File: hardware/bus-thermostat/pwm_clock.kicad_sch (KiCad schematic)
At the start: 16 parts, among them U12 NE555PWR, U14 TLV9301IDCK, U16 TLV9301IDCK

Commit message: Update some components
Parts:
- added TP1: TestPoint, Connector_Pin:Pin_D0.7mm_L6.5mm_W1.8mm_FlatFork, symbol Connector:TestPoint
- TP2: renamed from TP?; footprint (none) -> Connector_Pin:Pin_D0.7mm_L6.5mm_W1.8mm_FlatFork
- gave numbers to parts that had none: 2
- renumbered C27 to C26, C28 to C27, C30 to C28, C31 to C29, C32 to C30, R44 to R41, U12 to U11, U14 to U12, U16 to U13
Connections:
- net at C29.1, U12.3 (-), U12.4: now also TP1.1

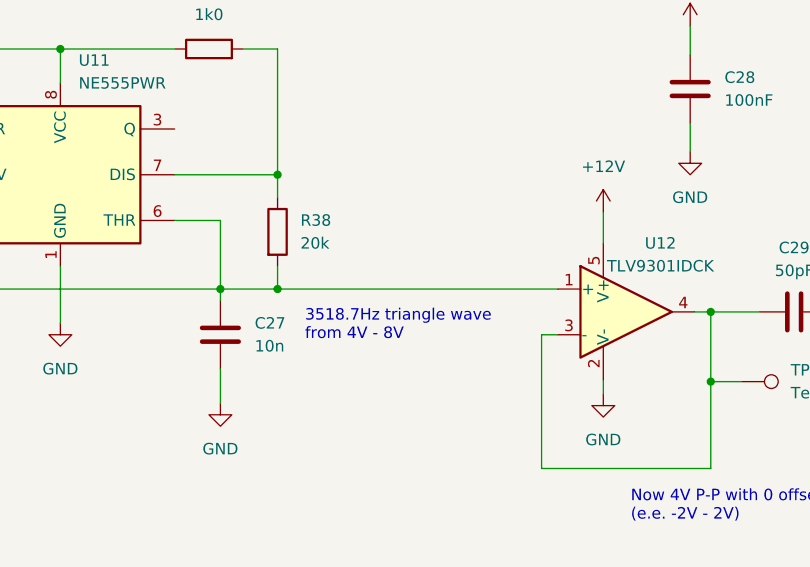
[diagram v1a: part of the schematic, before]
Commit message: Adjust PWMClock to 50kHz, use pulse transformers
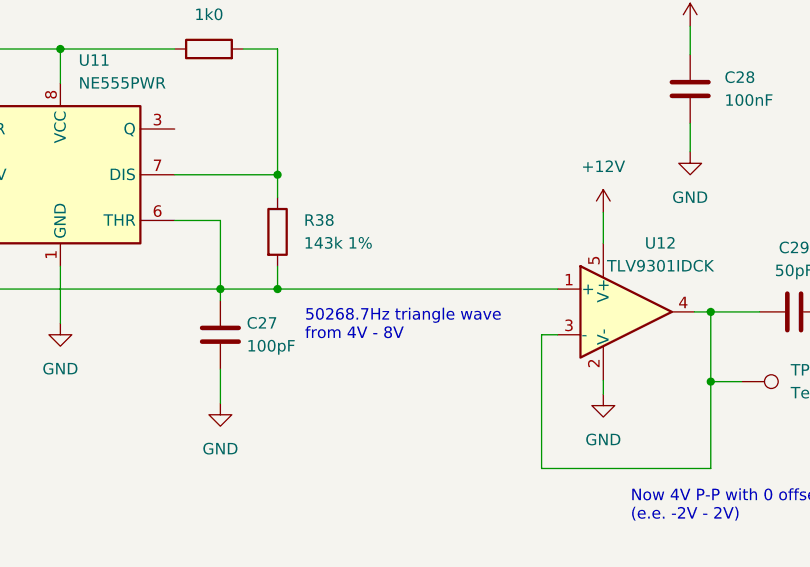
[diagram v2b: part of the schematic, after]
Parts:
- C27: value 10n -> 100pF
- R38: value 20k -> 143k 1%
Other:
- note added: "50268.7Hz triangle wave from 4V - 8V"
- note removed: "3518.7Hz triangle wave from 4V - 8V"
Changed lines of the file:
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@@
     (stroke (width 0) (type default) (color 0 0 0 0))
   )
-  (text "3518.7Hz triangle wave\nfrom 4V - 8V" (at 108.077 95.123 0)
+  (text "50268.7Hz triangle wave\nfrom 4V - 8V" (at 108.077 95.123 0)
     (effects (font (size 1.27 1.27)) (justify left bottom))
   )
@@
   (symbol (lib_id "Device:C") (at 98.679 94.361 0) (unit 1)
     (in_bom yes) (on_board yes) (fields_autoplaced)
-    (property "Reference" "C27" (id 0) (at 102.489 93.0909 0)
-      (effects (font (size 1.27 1.27)) (justify left))
-    )
-    (property "Value" "10n" (id 1) (at 102.489 95.6309 0)
+    (property "Reference" "C27" (id 0) (at 101.6 93.0909 0)
+      (effects (font (size 1.27 1.27)) (justify left))
+    )
+    (property "Value" "100pF" (id 1) (at 101.6 95.6309 0)
       (effects (font (size 1.27 1.27)) (justify left))
     )
@@
   (symbol (lib_id "Device:R") (at 105.029 82.931 0) (unit 1)
     (in_bom yes) (on_board yes) (fields_autoplaced)
-    (property "Reference" "R38" (id 0) (at 107.569 81.6609 0)
-      (effects (font (size 1.27 1.27)) (justify left))
-    )
-    (property "Value" "20k" (id 1) (at 107.569 84.2009 0)
-      (effects (font (size 1.27 1.27)) (justify left))
-    )
+    (property "Reference" "R38" (id 0) (at 107.95 81.6609 0)
+      (effects (font (size 1.27 1.27)) (justify left))
+    )
+    (property "Value" "143k 1%" (id 1) (at 107.95 84.2009 0)
+      (effects (font (size 1.27 1.27)) (justify left))
+    )

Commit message: More slight tweaks for resimulation
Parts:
- C29: value 50pF -> 10pF
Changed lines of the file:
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@@
   (symbol (lib_id "Device:C") (at 162.433 91.821 90) (unit 1)
     (in_bom yes) (on_board yes) (fields_autoplaced)
-    (property "Reference" "C29" (id 0) (at 162.433 84.709 90))
-    (property "Value" "50pF" (id 1) (at 162.433 87.249 90))
+    (property "Reference" "C29" (id 0) (at 162.433 83.82 90))
+    (property "Value" "10pF" (id 1) (at 162.433 86.36 90))
     (property "Footprint" "" (id 2) (at 166.243 90.8558 0)
       (effects (font (size 1.27 1.27)) hide)

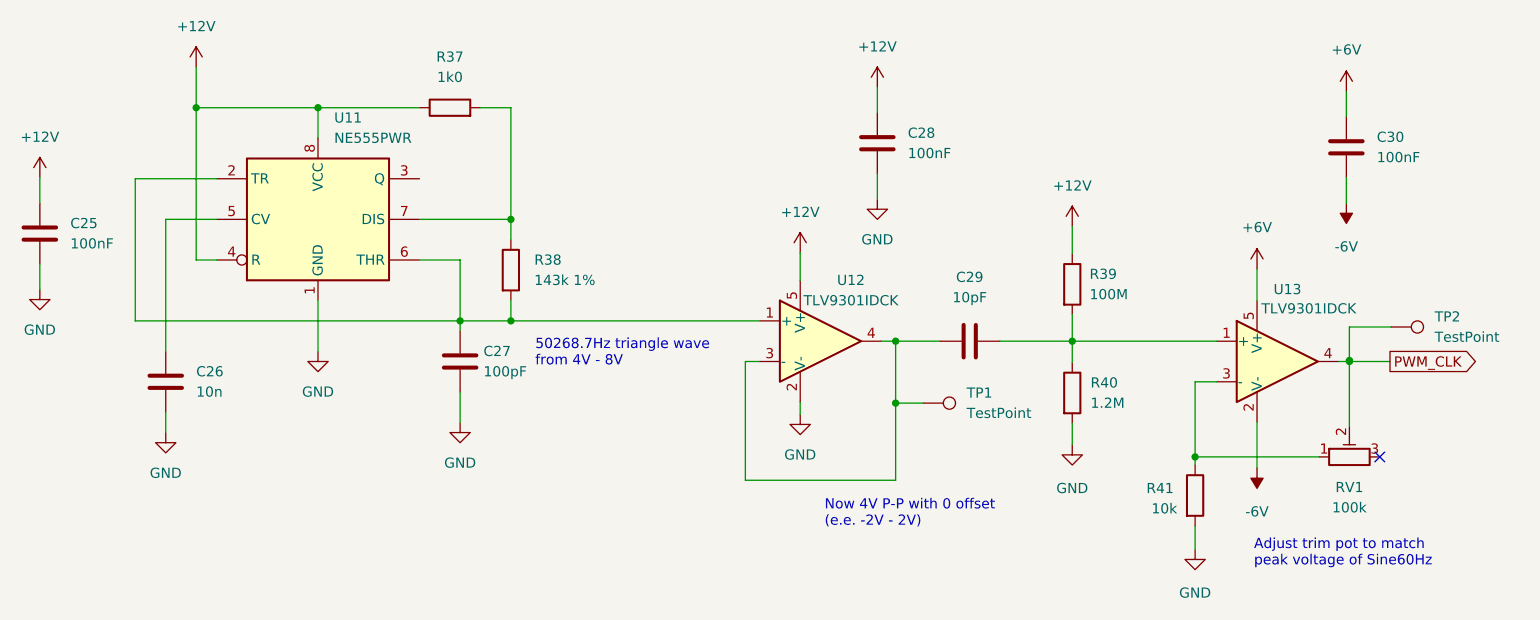
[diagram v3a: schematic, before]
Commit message: Fix oscillator, add fan controller/thermostat and its IOs.
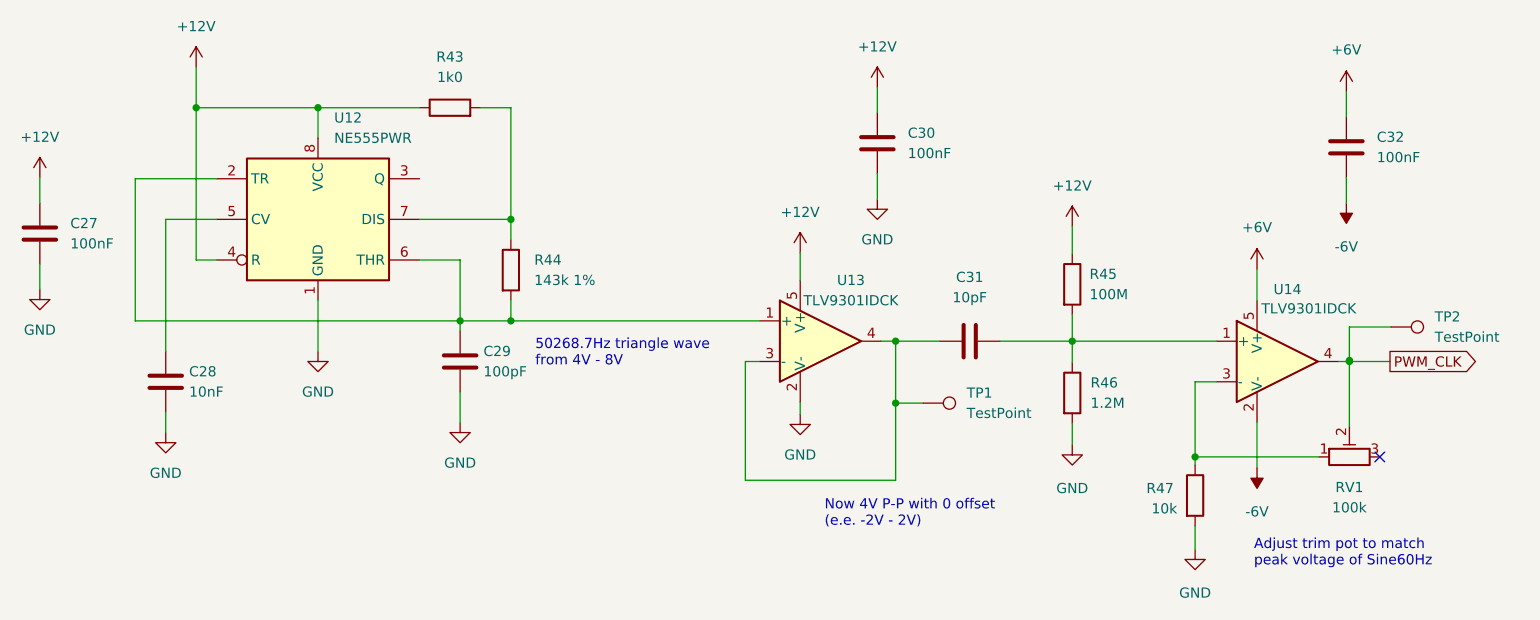
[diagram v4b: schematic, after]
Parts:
- C27: renamed from C25; footprint (none) -> Capacitor_SMD:C_0805_2012Metric_Pad1.18x1.45mm_HandSolder
- C28: renamed from C26; value 10n -> 10nF; footprint (none) -> Capacitor_SMD:C_0805_2012Metric_Pad1.18x1.45mm_HandSolder
- C29: renamed from C27; footprint (none) -> Capacitor_SMD:C_0805_2012Metric_Pad1.18x1.45mm_HandSolder
- C30: renamed from C28; footprint (none) -> Capacitor_SMD:C_0805_2012Metric_Pad1.18x1.45mm_HandSolder
- C31: renamed from C29; footprint (none) -> Capacitor_SMD:C_0805_2012Metric_Pad1.18x1.45mm_HandSolder
- C32: renamed from C30; footprint (none) -> Capacitor_SMD:C_0805_2012Metric_Pad1.18x1.45mm_HandSolder
- R43: renamed from R37; footprint (none) -> Resistor_SMD:R_0805_2012Metric_Pad1.20x1.40mm_HandSolder
- R44: renamed from R38; footprint (none) -> Resistor_SMD:R_0805_2012Metric_Pad1.20x1.40mm_HandSolder
- R45: renamed from R39; footprint (none) -> Resistor_SMD:R_0805_2012Metric_Pad1.20x1.40mm_HandSolder
- R46: renamed from R40; footprint (none) -> Resistor_SMD:R_0805_2012Metric_Pad1.20x1.40mm_HandSolder
- R47: renamed from R41; footprint (none) -> Resistor_SMD:R_0805_2012Metric_Pad1.20x1.40mm_HandSolder
- RV1: footprint (none) -> Resistor_SMD:R_0805_2012Metric_Pad1.20x1.40mm_HandSolder
- renumbered U11 to U12, U12 to U13, U13 to U14
